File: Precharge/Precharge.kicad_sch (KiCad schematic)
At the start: 69 parts, among them J2 Conn_01x02, J3 Conn_01x02, J4 Molex MicroFit, J5 Conn_02x03_Counter_Clockwise, K3 KT12-1A-40L-THT, Q1 CJ2310, Q2 AO3400A, Q3 AO3400A, U1 LM393, U2 4N35, U3 4N35

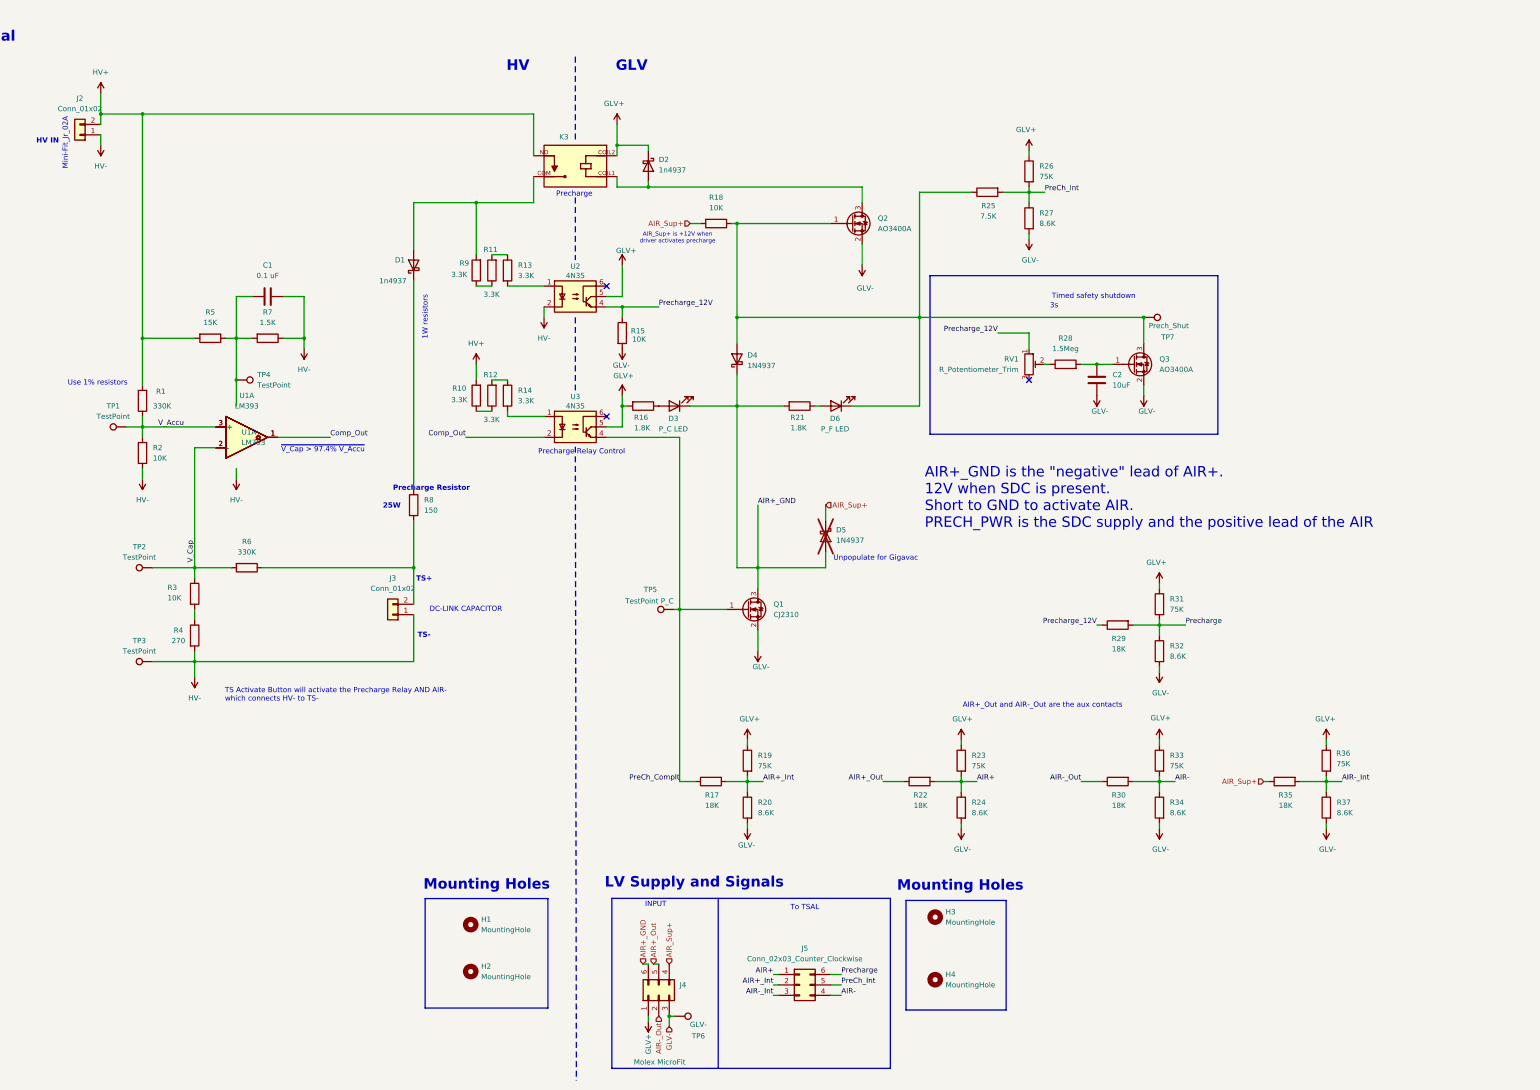
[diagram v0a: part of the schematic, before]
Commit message: Precharge: Add isolated DC-DC
New Precharge version
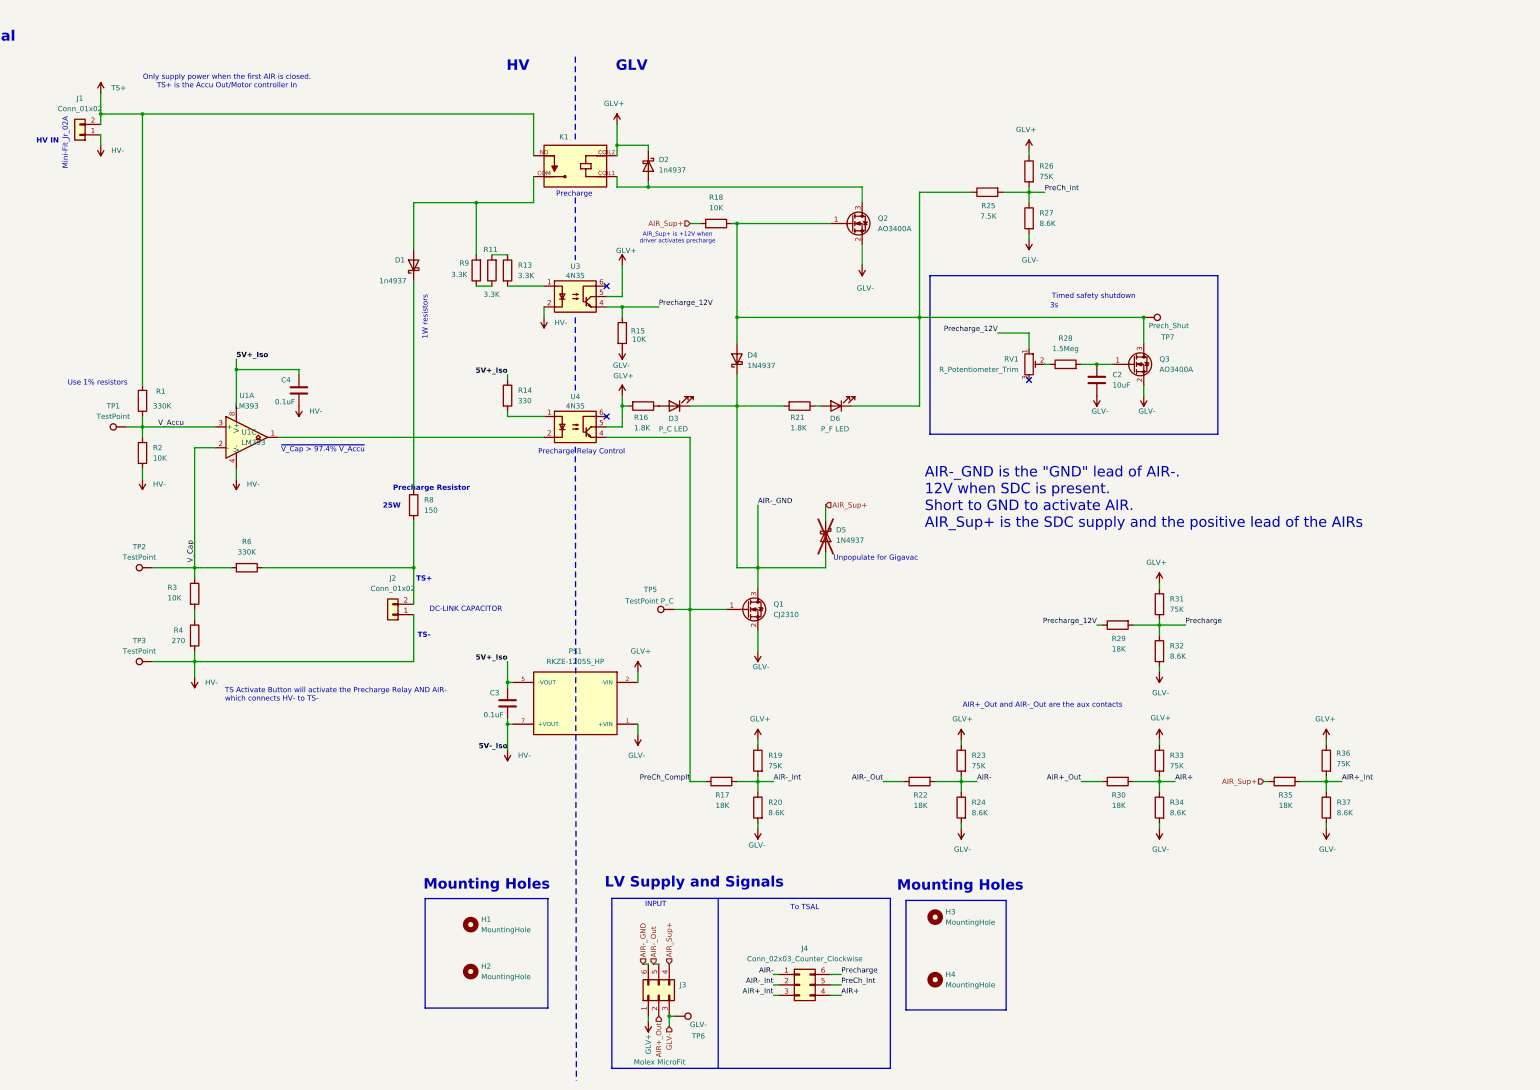
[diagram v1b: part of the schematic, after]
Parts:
- removed C1: 0.1 uF, Capacitor_SMD:C_0805_2012Metric_Pad1.18x1.45mm_HandSolder, symbol Device:C
- removed R10, R12: 3.3K, Resistor_SMD:R_2512_6332Metric_Pad1.40x3.35mm_HandSolder, symbol Device:R
- removed R5: 15K, Resistor_SMD:R_1206_3216Metric, symbol Device:R
- removed R7: 1.5K, Resistor_SMD:R_1206_3216Metric, symbol Device:R
- removed TP4: TestPoint, Connector_Pin:Pin_D1.0mm_L10.0mm, symbol Connector:TestPoint
- added C3, C4: 0.1uF, Capacitor_SMD:C_0603_1608Metric_Pad1.08x0.95mm_HandSolder, symbol Device:C
- added PS1: RKZE-1205S_HP, Recom DC-DC:CONV_RKZE-1205S_HP, symbol Recom 12V Isolated:RKZE-1205S_HP
- R14: value 3.3K -> 330; footprint Resistor_SMD:R_2512_6332Metric_Pad1.40x3.35mm_HandSolder -> Resistor_SMD:R_0805_2012Metric_Pad1.20x1.40mm_HandSolder
- renumbered J2 to J1, J3 to J2, J4 to J3, J5 to J4, K3 to K1, U2 to U3, U3 to U4
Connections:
- net AIR+: now also J4.4 (Pin_4), R30.2, R33.2, R34.1; no longer J4.1 (Pin_1), R22.2, R23.2, R24.1
- net AIR+_Int: now also J4.3 (Pin_3), R35.2, R36.2, R37.1; no longer J4.2 (Pin_2), R17.2, R19.2, R20.1
- net AIR+_Out: now also J3.2 (Pin_2), R30.1; no longer J3.5 (Pin_5), R22.1
- net AIR-: now also J4.1 (Pin_1), R22.2, R23.2, R24.1; no longer J4.4 (Pin_4), R30.2, R33.2, R34.1
- net AIR-_Int: now also J4.2 (Pin_2), R17.2, R19.2, R20.1; no longer J4.3 (Pin_3), R35.2, R36.2, R37.1
- net AIR-_Out: now also J3.5 (Pin_5), R22.1; no longer J3.2 (Pin_2), R30.1
- net GLV+: now also PS1.2 (-VIN)
- net GLV-: now also PS1.1 (+VIN)
- net HV-: now also U1.4 (V-), C3.2, C4.2, PS1.7 (+VOUT)
- net V_Accu: no longer U1.3 (+)
- net V_Cap: no longer U1.2 (-)
- net 5V+_Iso: now reaches R14.1
- net 5V+_Iso: now also U1.8 (V+), C3.1, C4.1, PS1.5 (-VOUT)
- net AIR+_GND renamed AIR-_GND
- net Comp_Out: no longer names the net of U1.1, U4.2
- net Comp_Out: no longer U1.1
- net HV+ renamed TS+
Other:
- note added: "AIR-_GND is the "GND" lead of AIR-. 12V when SDC is present. Short to GND to activate AIR. AIR_Sup+ is the SDC supply and the positive lead of the AIRs"
- note added: "Only supply power when the first AIR is closed. TS+ is the Accu Out/Motor controller In"
- note removed: "AIR+_GND is the "negative" lead of AIR+. 12V when SDC is present. Short to GND to activate AIR. PRECH_PWR is the SDC supply and the positive lead of the AIR"
- moved on the sheet: R17, R19, R20

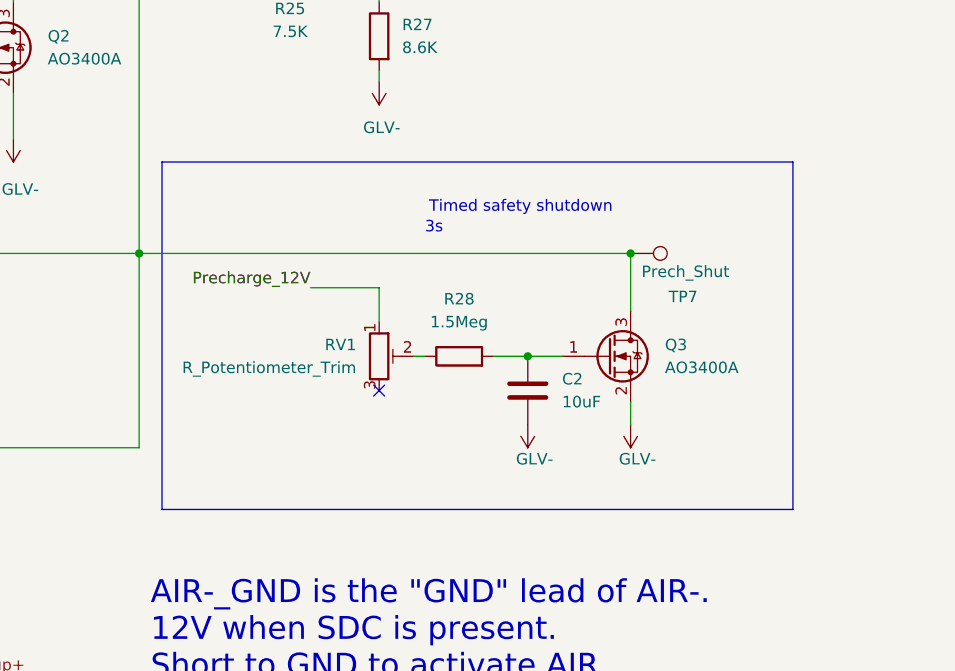
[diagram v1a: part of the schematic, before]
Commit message: Precharge: cap DC bias correction, PDs on TSAL
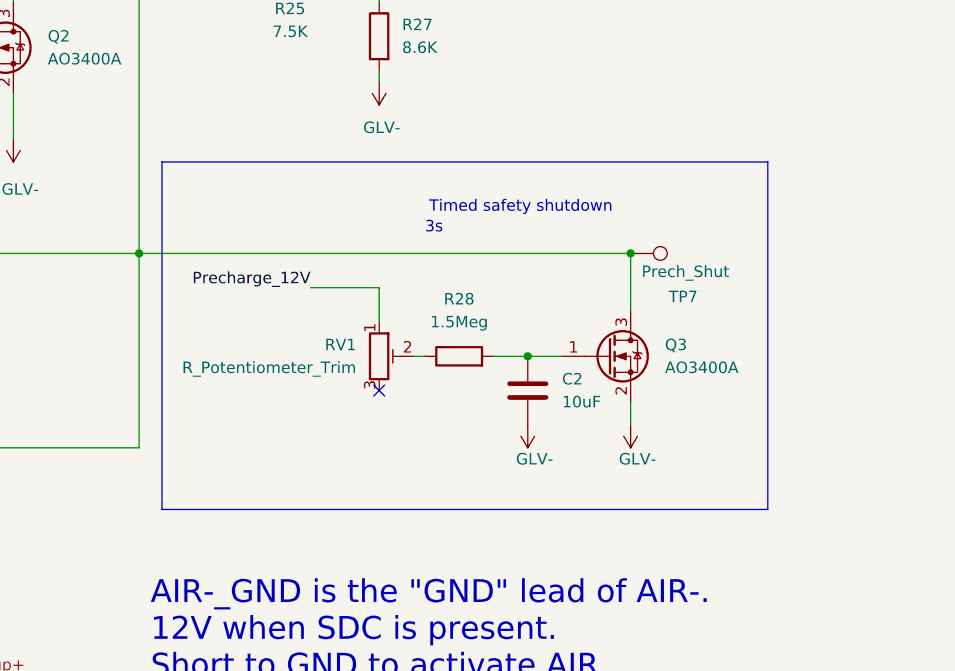
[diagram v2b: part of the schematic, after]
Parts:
- C2: footprint Capacitor_SMD:C_0805_2012Metric_Pad1.18x1.45mm_HandSolder -> Capacitor_SMD:C_Elec_4x5.4
- R28: footprint Resistor_SMD:R_0603_1608Metric_Pad0.98x0.95mm_HandSolder -> Resistor_SMD:R_0805_2012Metric_Pad1.20x1.40mm_HandSolder
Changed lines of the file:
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@@
 		(title "Precharge Circuit")
 		(date "2026-05-11")
-		(rev "5.0")
+		(rev "5.1")
 		(company "Formula Barton Racing")
 		(comment 1 "evanscesil@gmail.com")
@@
 	(rectangle
 		(start 276.86 87.63)
-		(end 346.964 126.238)
+		(end 344.17 126.238)
 		(stroke
 			(width 0)
@@
 			)
 		)
-		(property "Footprint" "Capacitor_SMD:C_0805_2012Metric_Pad1.18x1.45mm_HandSolder"
+		(property "Footprint" "Capacitor_SMD:C_Elec_4x5.4"
 			(at 318.4652 116.84 0)
 			(hide yes)
@@
 			)
 		)
-		(property "Footprint" "Resistor_SMD:R_0603_1608Metric_Pad0.98x0.95mm_HandSolder"
+		(property "Footprint" "Resistor_SMD:R_0805_2012Metric_Pad1.20x1.40mm_HandSolder"
 			(at 309.88 110.998 90)
 			(hide yes)
